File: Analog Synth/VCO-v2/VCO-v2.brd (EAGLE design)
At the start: 100 x 100 mm, 64 parts, among them IC1 TL084P, IC2 TL084P, IC3 78L09, IC5 79L09\, Q1 J310, Q2 J310, T1 2N3904, T2 2N3904, T3 2N3904, T4 2N3904, T7 2N3904, U1 CA3096

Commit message: VCO-v2 PWM and Triangle outputs
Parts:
- added C10, C9: 100u, rcl:E3,5-10
- added C11, C13, C16, C17: 10u, rcl:E3,5-10
- added C12, C14, C15, C18, C19, C20, C21: 0.1u, resistor:C025-050X050
- added CV-PWM, PWM, TRIANGLE: I/O, !synth_sch:MONO_JACK
- added IC7: TL084P, linear:DIL14
- added PWM-MAN: 100k lin, pot:B64Y
- added R30, R31: 10k, resistor:0204/7
- added R32, R35, R36: 2.2k, resistor:0204/7
- added R33, R34, R38: 100k, resistor:0204/7
- added R37: 47k, resistor:0204/7
- C8: value 100p -> 0.1u
- FREQ-MAN: value 10k -> 10k lin
- IC4: value (none) -> 78L05
- IC6: value (none) -> 79L05
- moved IC3 60.8 mm to (5.08, 55.9)
- moved R28 60.8 mm to (7.62, 26.7)
- moved C8 60.8 mm to (5.08, 34.3)
- moved IC4 60.8 mm to (5.08, 50.8)
- moved IC5 60.8 mm to (5.08, 45.7)
- moved IC6 60.8 mm to (5.08, 40.6)
- moved R29 60.8 mm to (7.62, 22.9)
- moved U$3 60.8 mm to (6.35, 69.8)
- renumbered CV_MANUAL to FREQ-MAN, CV_MANUAL1 to ATTN_CV_B, CV_MANUAL2 to ATTN_CV_C
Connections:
- new net N$27: IC2.9, R30.2, R31.2
- new net N$28: R32.1, TRIANGLE.P$2
- new net N$36: C21.1
- new net N$37: IC2.14, R35.1
- new net N$38: PWM.P$2, R35.2, R36.2
- new net N$39: IC7.5, R37.2
- new net N$40: IC7.6, IC7.7, R34.1
- new net N$41: CV-PWM.P$2, R37.1
- new net N$43: IC7.2, R33.2, R34.2, R38.1
- new net N$44: IC2.13, IC7.1, R38.2
- new net N$45: PWM-MAN.S, R33.1
- new net TRIANGLE: IC2.12, IC2.8, R31.1, R32.2
- net +12V: now also C14.1, C8.1, C9.+, IC1.4, IC2.4
- net +5V: now also C17.+, C19.1, PWM-MAN.A
- net +9V: now also C11.+, C18.1
- net -12V: now also C10.+, C12.1, C15.1, IC1.11, IC2.11
- net -5V: now also C16.+, PWM-MAN.E
- net -9V: now also C13.+, C20.1
- net GND: now also C10.-, C11.-, C12.2, C13.-, C14.2, C15.2, C16.-, C17.-, C18.2, C19.2, C20.2, C21.2, C8.2, C9.-, CV-PWM.P$1, CV-PWM.P$3, IC5.GND, IC7.3, PWM.P$1, R30.1, R36.1, TRIANGLE.P$1
- net V+: now also IC7.4; no longer IC1.4, IC2.4
- net V-: now also IC7.11; no longer IC1.11, IC2.11
- net V-CAP-BUFF: now also IC2.10

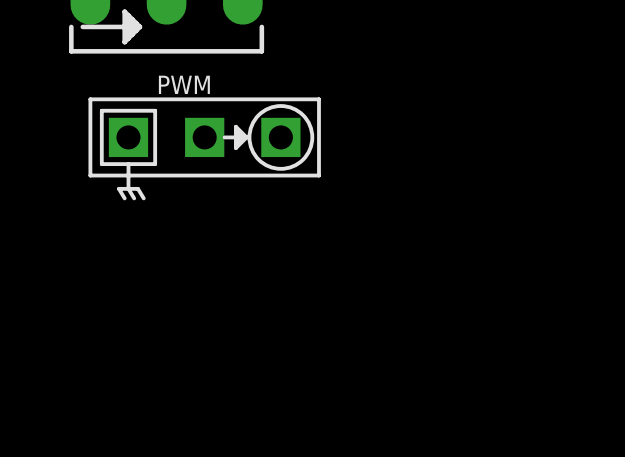
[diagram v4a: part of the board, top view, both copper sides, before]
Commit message: VCO-v2 PWM control voltage attenuation
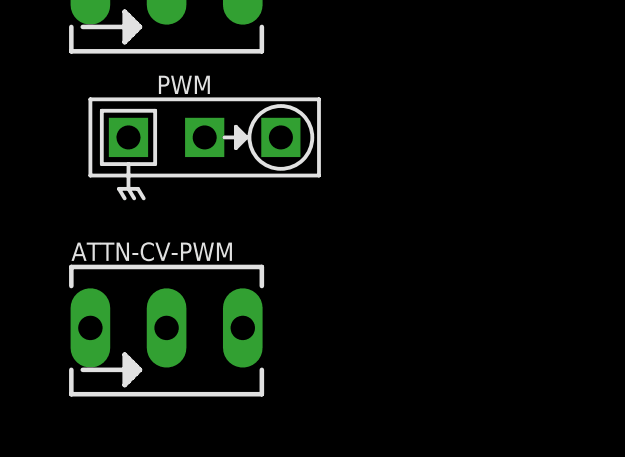
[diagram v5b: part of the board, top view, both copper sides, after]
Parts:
- added ATTN-CV-PWM: 100k lin, pot:B64Y
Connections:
- new net N$42: ATTN-CV-PWM.S, R34.1
- net GND: now also ATTN-CV-PWM.A
- net N$40: now also ATTN-CV-PWM.E; no longer R34.1
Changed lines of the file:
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@@
 <element name="PWM-MAN" library="pot" package="B64Y" value="100k lin" x="-83.82" y="-172.72"/>
 <element name="PWM" library="!synth_sch" package="MONO_JACK" value="I/O" x="-82.55" y="-177.8"/>
+<element name="ATTN-CV-PWM" library="pot" package="B64Y" value="100k lin" x="-83.82" y="-184.15"/>
 </elements>
 <signals>
@@
 <contactref element="IC7" pad="3"/>
 <contactref element="PWM" pad="P$1"/>
+<contactref element="ATTN-CV-PWM" pad="A"/>
 <wire x1="-82.55" y1="-162.56" x2="-85.09" y2="-162.56" width="0" layer="19" extent="1-1"/>
 <wire x1="-86.36" y1="-154.94" x2="-85.09" y2="-162.56" width="0" layer="19" extent="1-1"/>
 <wire x1="-85.09" y1="-177.8" x2="-85.09" y2="-162.56" width="0" layer="19" extent="1-1"/>
+<wire x1="-81.28" y1="-184.15" x2="-85.09" y2="-177.8" width="0" layer="19" extent="1-1"/>
 <wire x1="-78.74" y1="-138.43" x2="-86.36" y2="-154.94" width="0" layer="19" extent="1-1"/>
 <wire x1="-85.09" y1="-121.92" x2="-78.74" y2="-138.43" width="0" layer="19" extent="1-1"/>
@@
 <contactref element="IC7" pad="6"/>
 <contactref element="IC7" pad="7"/>
-<contactref element="R34" pad="1"/>
-<wire x1="-71.12" y1="-138.43" x2="-86.36" y2="-147.32" width="0" layer="19" extent="1-1"/>
+<contactref element="ATTN-CV-PWM" pad="E"/>
 <wire x1="-68.58" y1="-138.43" x2="-71.12" y2="-138.43" width="0" layer="19" extent="1-1"/>
+<wire x1="-86.36" y1="-184.15" x2="-71.12" y2="-138.43" width="0" layer="19" extent="1-1"/>
 </signal>
 <signal name="N$41">
@@
 <wire x1="-83.82" y1="-172.72" x2="-86.36" y2="-143.51" width="0" layer="19" extent="1-1"/>
 </signal>
+<signal name="N$42">
+<contactref element="R34" pad="1"/>
+<contactref element="ATTN-CV-PWM" pad="S"/>
+<wire x1="-83.82" y1="-184.15" x2="-86.36" y2="-147.32" width="0" layer="19" extent="1-1"/>
+</signal>
 </signals>

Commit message: VCO-v2 Sine (from VCO-v1 basically)
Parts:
- added Q3, Q4: 2N3904, transistor-npn:TO92
- added R-SINE-AMPL, R-SINE-ROUND: 100k lin, pot:B64Y
- added R-SINE-SYMM: 10 kΩ, pot:B64Y
- added R39, R40: 2.2 kΩ, resistor:0204/7
- added R41: 390 Ω, resistor:0204/7
- added R42: 18 kΩ, resistor:0204/7
- added R43, R44, R45, R46: 10 kΩ, resistor:0204/7
- added R47: 1k, resistor:0204/7
- added SINE: I/O, !synth_sch:MONO_JACK
- R32: value 2.2k -> 1k
- moved PWM-MAN 311.9 mm to (73.7, 96.5)
- moved R38 300.8 mm to (72.4, 90.2)
- moved R32 244.0 mm to (38.1, 85.1), turned to 180 degrees
- moved ATTN-CV-PWM 228.9 mm to (19.1, 20.3)
- moved PWM 228.3 mm to (19.1, 26.7)
- moved CV-PWM 227.6 mm to (38.1, 30.5)
- moved R33 227.6 mm to (38.1, 49.5)
- moved R34 227.6 mm to (38.1, 45.7)
- moved R35 227.6 mm to (38.1, 41.9)
- moved R36 227.6 mm to (38.1, 38.1)
- moved R37 227.6 mm to (38.1, 34.3)
- moved R30 225.3 mm to (29.2, 81.3)
- moved R31 224.6 mm to (27.9, 77.5)
- moved TRIANGLE 224.6 mm to (27.9, 73.7)
- moved IC7 218.2 mm to (76.2, 21.6)
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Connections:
- net N$37 renamed PWM
- new net N$37: Q3.2, R-SINE-ROUND.E, R39.1
- new net N$46: Q4.2, R40.1
- new net N$47: Q3.3, R-SINE-SYMM.A, R41.1
- new net N$48: Q4.3, R-SINE-SYMM.E, R41.2
- new net N$49: R-SINE-SYMM.S, R42.1
- new net N$50: IC7.9, Q3.1, R43.1, R46.1
- new net N$51: IC7.8, R-SINE-AMPL.A, R46.2
- new net N$52: IC7.10, Q4.1, R44.1, R45.2
- new net N$54: IC7.13, R-SINE-AMPL.S
- new net N$55: R47.2, SINE.P$2
- new net SINE: IC7.14, R-SINE-AMPL.E, R47.1
- net +9V: now also R43.2, R44.2
- net -9V: now also R42.2
- net GND: now also IC7.12, R39.2, R40.2, R45.1, SINE.P$1
- net TRIANGLE: now also R-SINE-ROUND.A, R-SINE-ROUND.S

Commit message: VCO-v2 LEDs sheet and signal names
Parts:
- added LED-CV-A, LED-CV-B, LED-CV-PWM, LED-PWM, LED-SINE, LED-TRIANGLE, LED_CV-C: (no value), led:LED3MM
- added R48, R49, R50, R51, R53, R54, R56: 4.7 kΩ, resistor:0204/7
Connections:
- removed net N$11: IC1.8, IC1.9, R6.1
- removed net N$5: IC1.6, IC1.7, R5.1
- removed net N$7: IC1.1, IC1.2, R4.1
- new net CV-A: IC1.1, IC1.2, LED-CV-A.A, R4.1
- new net CV-B: IC1.6, IC1.7, LED-CV-B.A, R5.1
- new net CV-C: IC1.8, IC1.9, LED_CV-C.A, R6.1
- new net CV-PWM: IC2.13, IC7.1, LED-CV-PWM.K, R38.2
- new net N$53: LED-CV-A.K, R48.1
- new net N$56: LED-CV-B.K, R49.1
- new net N$57: LED_CV-C.K, R50.1
- new net N$59: LED-PWM.K, R53.1
- new net N$60: LED-TRIANGLE.K, R56.1
- new net N$61: LED-SINE.K, R54.1
- net -5V: now also R48.2, R49.2, R50.2, R51.2, R53.2, R54.2, R56.2
- net N$3: now also IC1.10, IC1.5
- net N$44: now also LED-CV-PWM.A, R51.1; no longer IC2.13, IC7.1, R38.2
- net PWM: now also LED-PWM.A
- net SINE: now also LED-SINE.A
- net TRIANGLE: now also LED-TRIANGLE.A

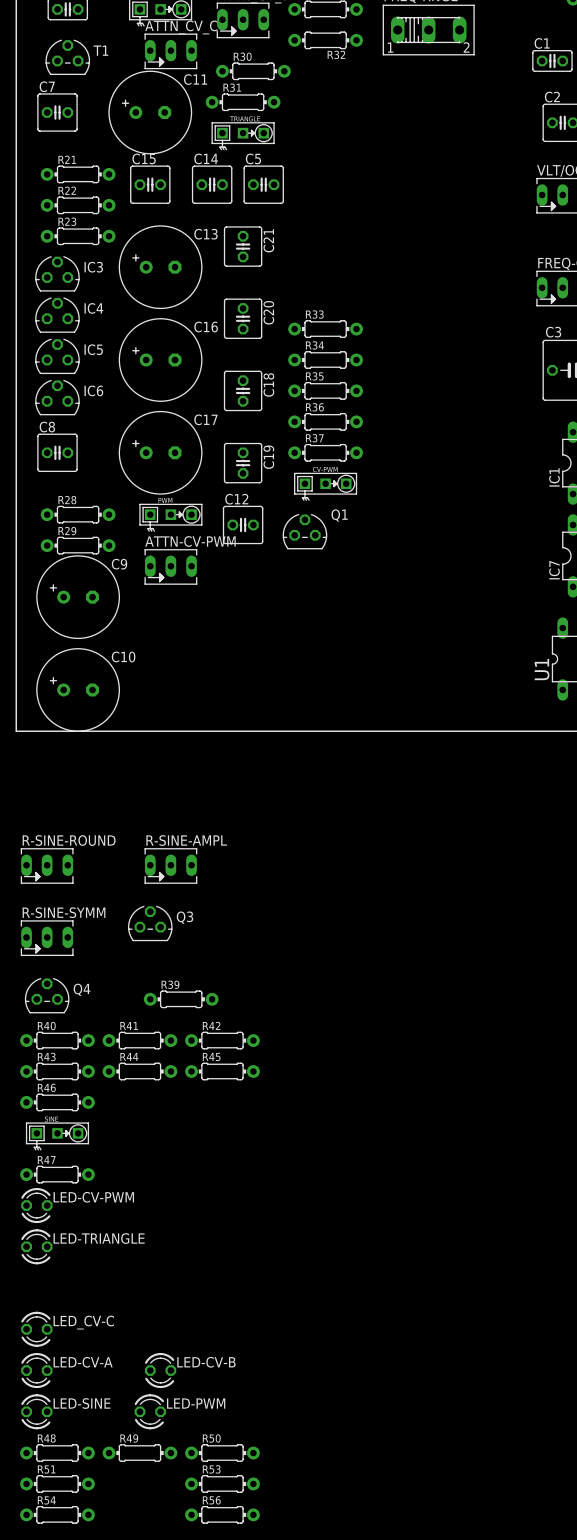
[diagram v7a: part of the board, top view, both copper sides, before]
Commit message: VCO-v2 - version 2.1 released! I changed a few things with the triangle-to-freq converter; I made the LEDs go into a bjt voltage source rather than the +5 V and -5 V regulated supplies, because connecting LEDs to those supply lines changed the frequency, and I'm not interested in that.
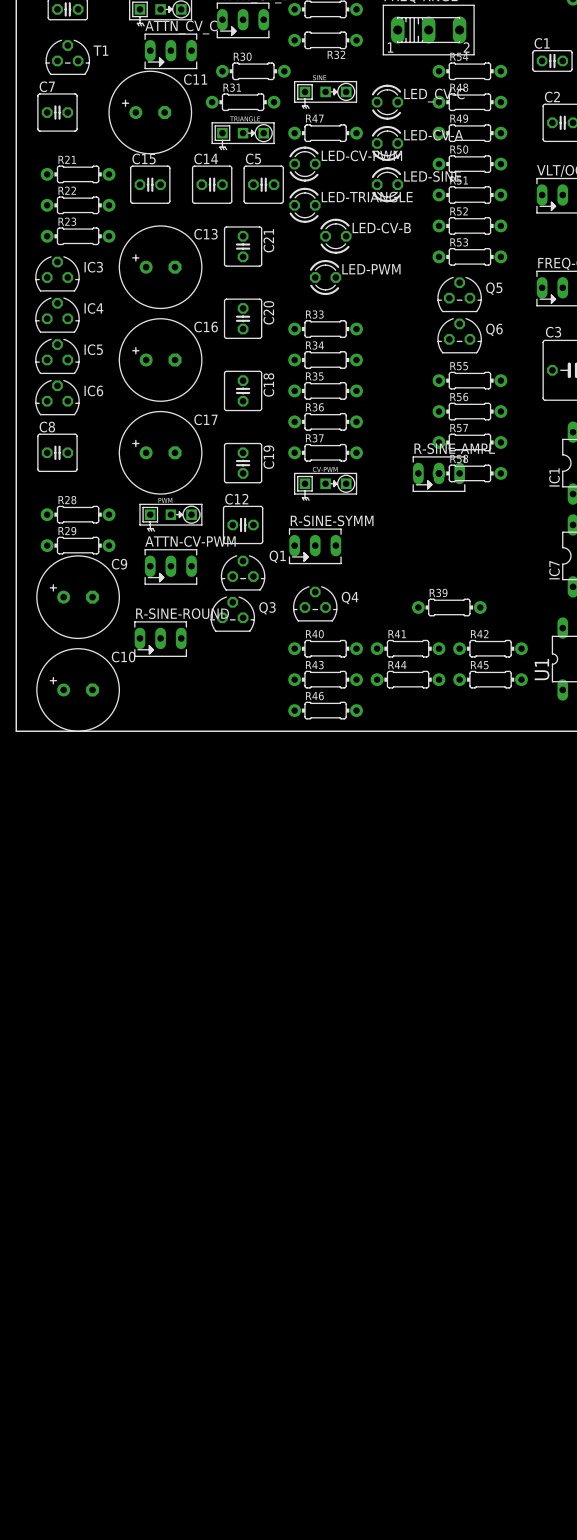
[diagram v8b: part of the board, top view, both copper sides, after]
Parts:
- added Q5: 2N3904, transistor-npn:TO92
- added Q6: 2N3906, transistor-pnp:TO92
- added R52: 4.7k, resistor:0204/7
- added R55, R58: 33k, resistor:0204/7
- added R57: 47k, resistor:0204/7
- ATTN-CV-PWM: value 100k lin -> 100k log
- R-SINE-AMPL, R-SINE-ROUND: value 100k lin -> 100k trim
- R-SINE-SYMM: value 10 kΩ -> 10k trim
- R39, R40: value 2.2 kΩ -> 2.2k
- R41: value 390 Ω -> 470
- R42: value 18 kΩ -> 100k
- R43, R44: value 10 kΩ -> 47k
- R45, R46: value 10 kΩ -> 10k
- R48, R49, R50, R51, R53, R54: value 4.7 kΩ -> 4.7k
- R56: value 4.7 kΩ -> 47k
- moved R54 184.9 mm to (55.9, 81.3)
- moved R48 174.0 mm to (55.9, 77.5)
- moved R49 167.6 mm to (55.9, 73.7)
- moved R51 166.7 mm to (55.9, 66.0)
- moved R50 161.6 mm to (55.9, 69.8)
- moved LED-CV-A 157.2 mm to (45.7, 72.4)
- moved LED-SINE 157.2 mm to (45.7, 67.3)
- moved LED_CV-C 157.2 mm to (45.7, 77.5)
- moved R53 154.2 mm to (55.9, 58.4)
- moved LED-CV-B 141.4 mm to (39.4, 61.0)
- moved LED-PWM 141.4 mm to (38.1, 55.9)
- moved R56 139.3 mm to (55.9, 39.4)
- moved LED-CV-PWM 132.5 mm to (35.6, 69.8)
- moved LED-TRIANGLE 132.5 mm to (35.6, 64.8)
- moved R47 132.5 mm to (38.1, 73.7)
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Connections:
- new net N$11: LED-CV-PWM.K, R53.1
- new net N$5: Q6.2, R55.1, R56.2
- new net N$58: LED-CV-PWM.A, Q5.3
- new net N$7: Q6.3, R48.2, R49.2, R50.2, R51.2, R52.2, R54.2
- net +12V: now also Q5.1, R58.1
- net -12V: now also Q6.1, R55.2
- net -5V: no longer R48.2, R49.2, R50.2, R51.2, R53.2, R54.2, R56.2
- net CV-PWM: now also R53.2; no longer LED-CV-PWM.K
- net GND: now also R56.1, R57.2
- net N$44: now also Q5.2, R57.1, R58.2; no longer LED-CV-PWM.A, R51.1
- net N$53: now also R52.1; no longer R48.1
- net N$56: now also R51.1; no longer R49.1
- net N$59: now also R48.1; no longer R53.1
- net N$60: now also R49.1; no longer R56.1
